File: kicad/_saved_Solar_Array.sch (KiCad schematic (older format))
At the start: 26 parts, among them IC1 SPV1040, P1 PV_CELL, P2 CONN_01X07, Q1 Q_NPN_BCE, U1 LTC2990

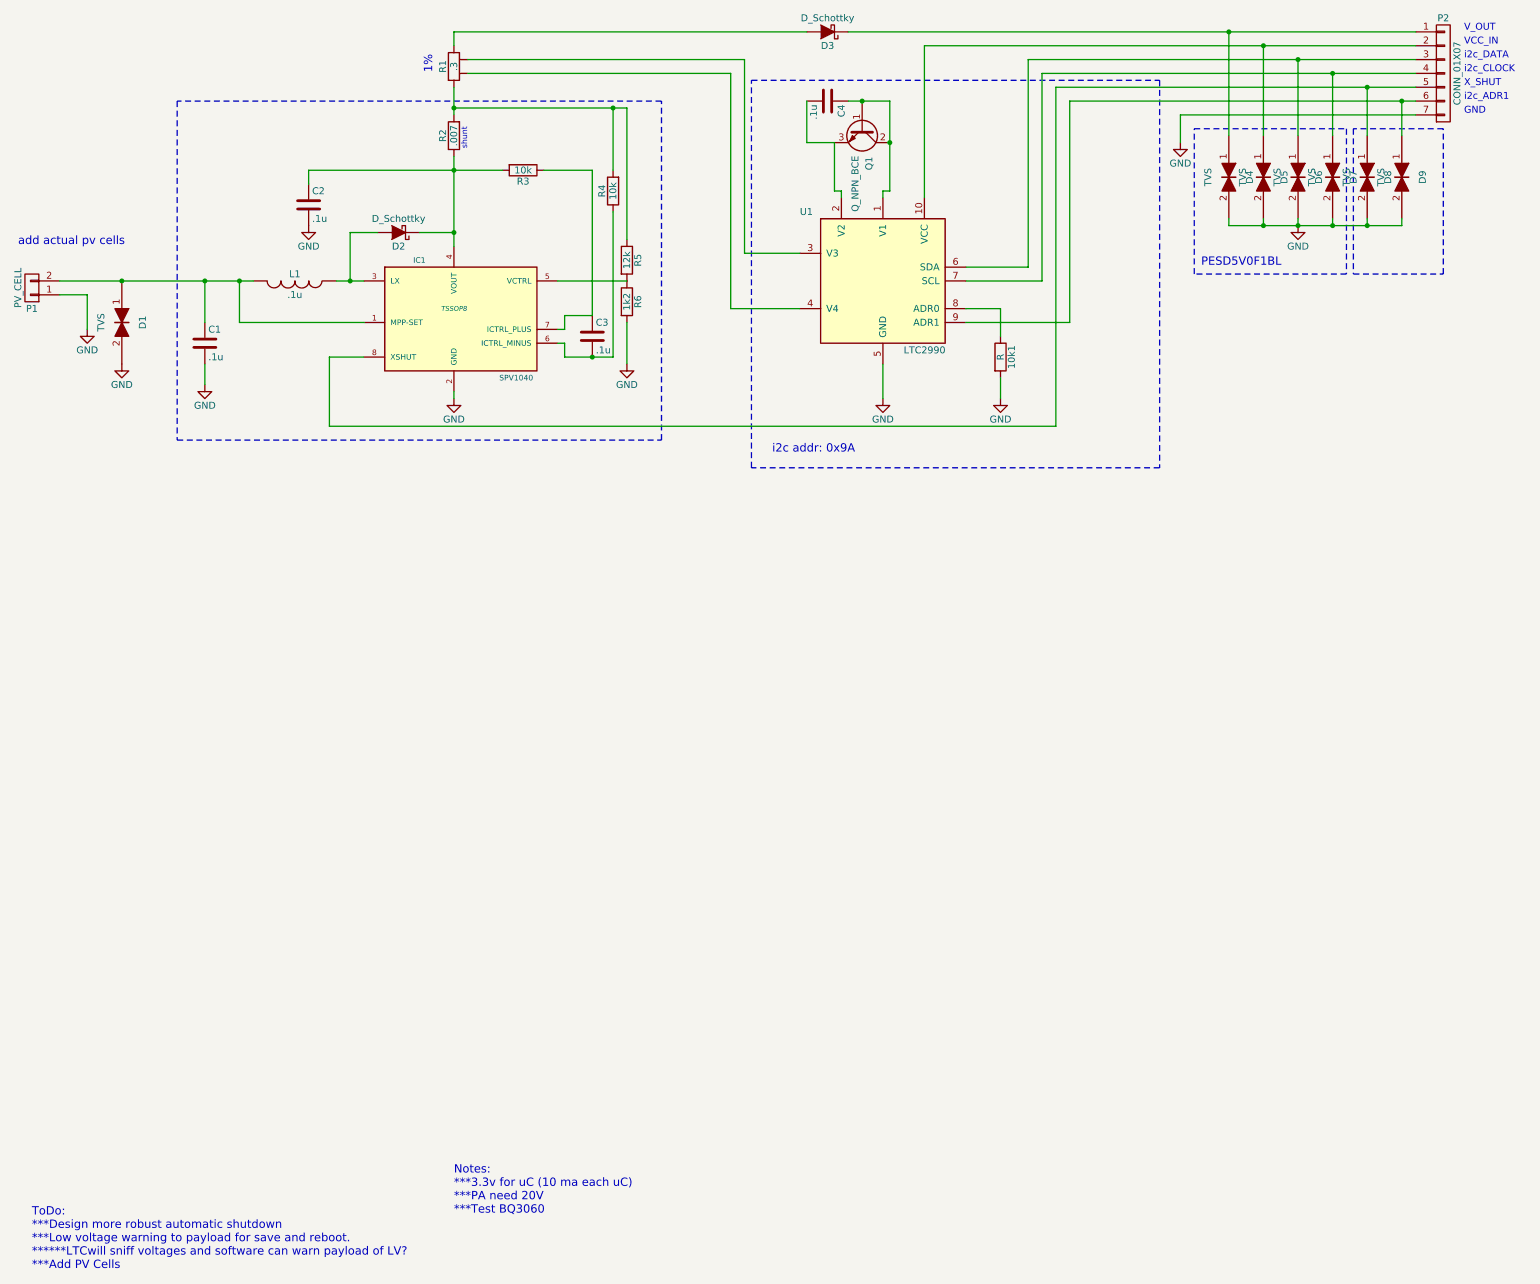
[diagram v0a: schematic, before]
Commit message: Update component values, generated netlist, changed notes.
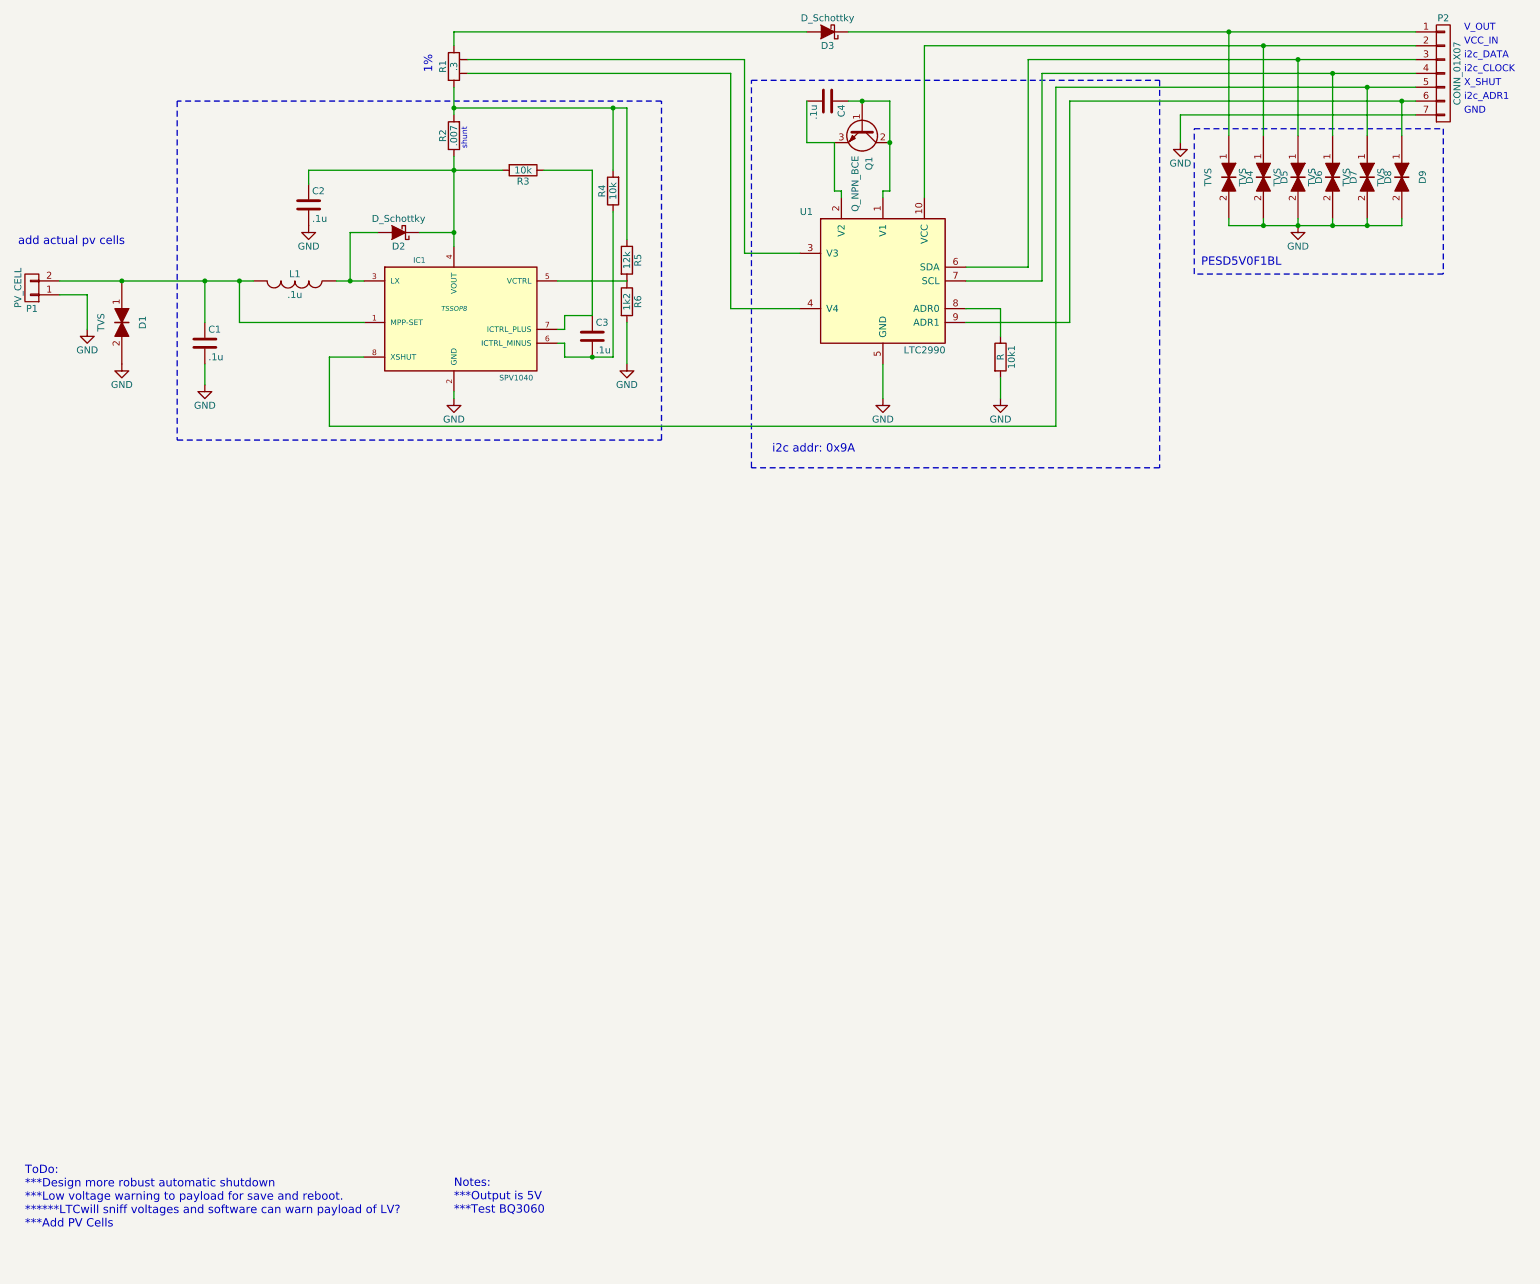
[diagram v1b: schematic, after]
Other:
- note added: "Notes:\n***Output is 5V\n***Test BQ3060"
- note removed: "Notes:\n***3.3v for uC (10 ma each uC)\n***PA need 20V\n***Test BQ3060"
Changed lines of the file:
@@
 	0    1    1    0
 $EndComp
-Text Notes 850  9900 0    60   ~ 0
+Text Notes 800  9600 0    60   ~ 0
 ToDo:\n***Design more robust automatic shutdown\n***Low voltage warning to payload for save and reboot.\n******LTCwill sniff voltages and software can warn payload of LV?\n***Add PV Cells
 Text Notes 3750 1250 1    60   ~ 0
@@
 VCC_IN
 Text Notes 3900 9500 0    60   ~ 0
-Notes:\n***3.3v for uC (10 ma each uC)\n***PA need 20V\n***Test BQ3060
+Notes:\n***Output is 5V\n***Test BQ3060
 Text Notes 11200 950  0    50   ~ 0
 V_OUT
@@
 $EndComp
 Wire Notes Line
-	9250 1650 10350 1650
-Wire Notes Line
-	10350 1650 10350 2700
-Wire Notes Line
-	10350 2700 9250 2700
+	9250 1650 11050 1650
 Wire Notes Line
 	9250 2700 9250 1650
 Wire Notes Line
-	10400 1650 10400 2700
-Wire Notes Line
-	10400 2700 11050 2700
-Wire Notes Line
-	11050 2700 11050 1650
-Wire Notes Line
-	11050 1650 10400 1650
+	11050 1650 11050 2700
 Text Notes 9300 2650 0    60   ~ 0
 PESD5V0F1BL
@@
 Wire Wire Line
 	7850 2950 7850 3150
+Wire Notes Line
+	11050 2700 9250 2700
 $EndSCHEMATC
